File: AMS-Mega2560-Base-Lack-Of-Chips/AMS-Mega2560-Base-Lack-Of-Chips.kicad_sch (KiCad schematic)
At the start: 22 parts, among them J1 RTD1, J2 RTD2, J3 Conn_01x08, J4 Sense1, J5 Sense2, J6 AdafruitUltimateGPS, J7 Conn_02x03_Odd_Even, P1 Power, P10 CONN_01X01, P11 CONN_01X01, P12 CONN_01X01, P13 CONN_01X01, P2 Analog, P3 Analog, P4 Digital, P5 PWM, P6 PWM, P7 Communication, P8 CONN_01X01, P9 CONN_01X01

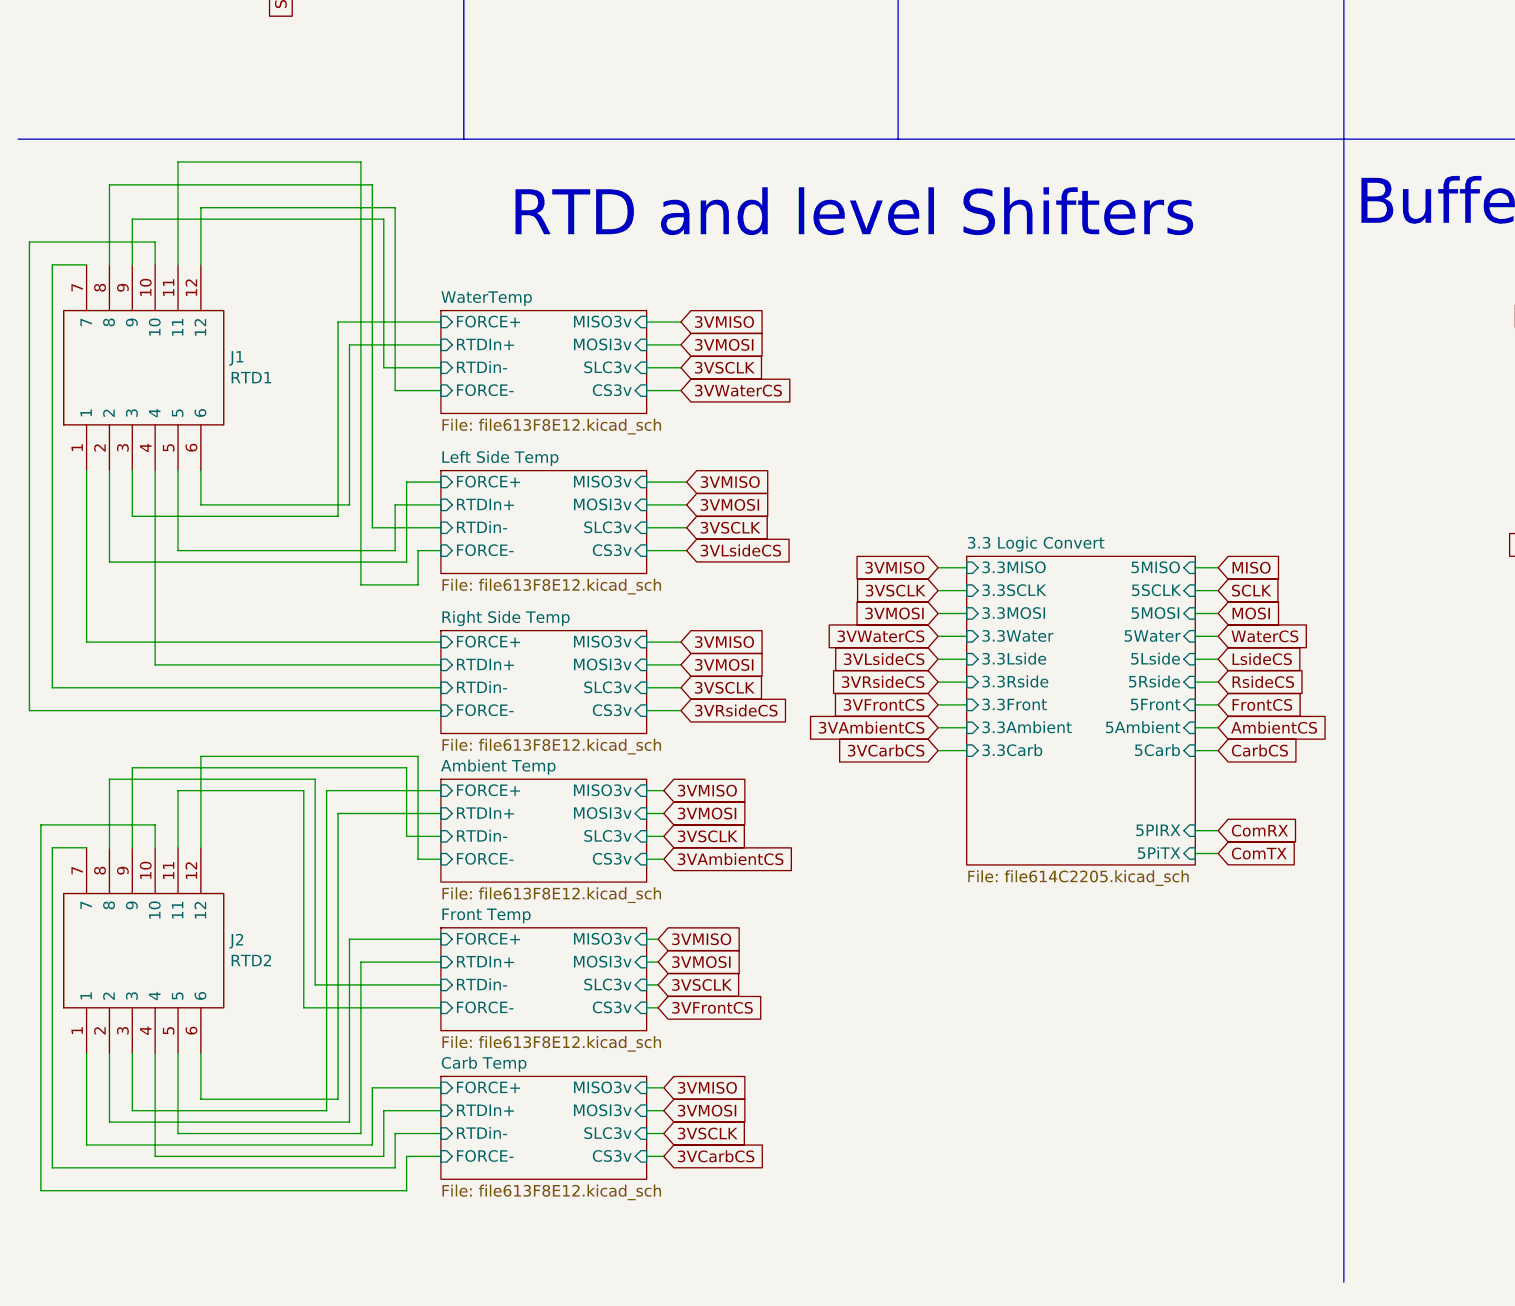
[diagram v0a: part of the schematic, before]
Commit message: replaced the RTD with adafruit Dev boards which are easy to get at the moment.
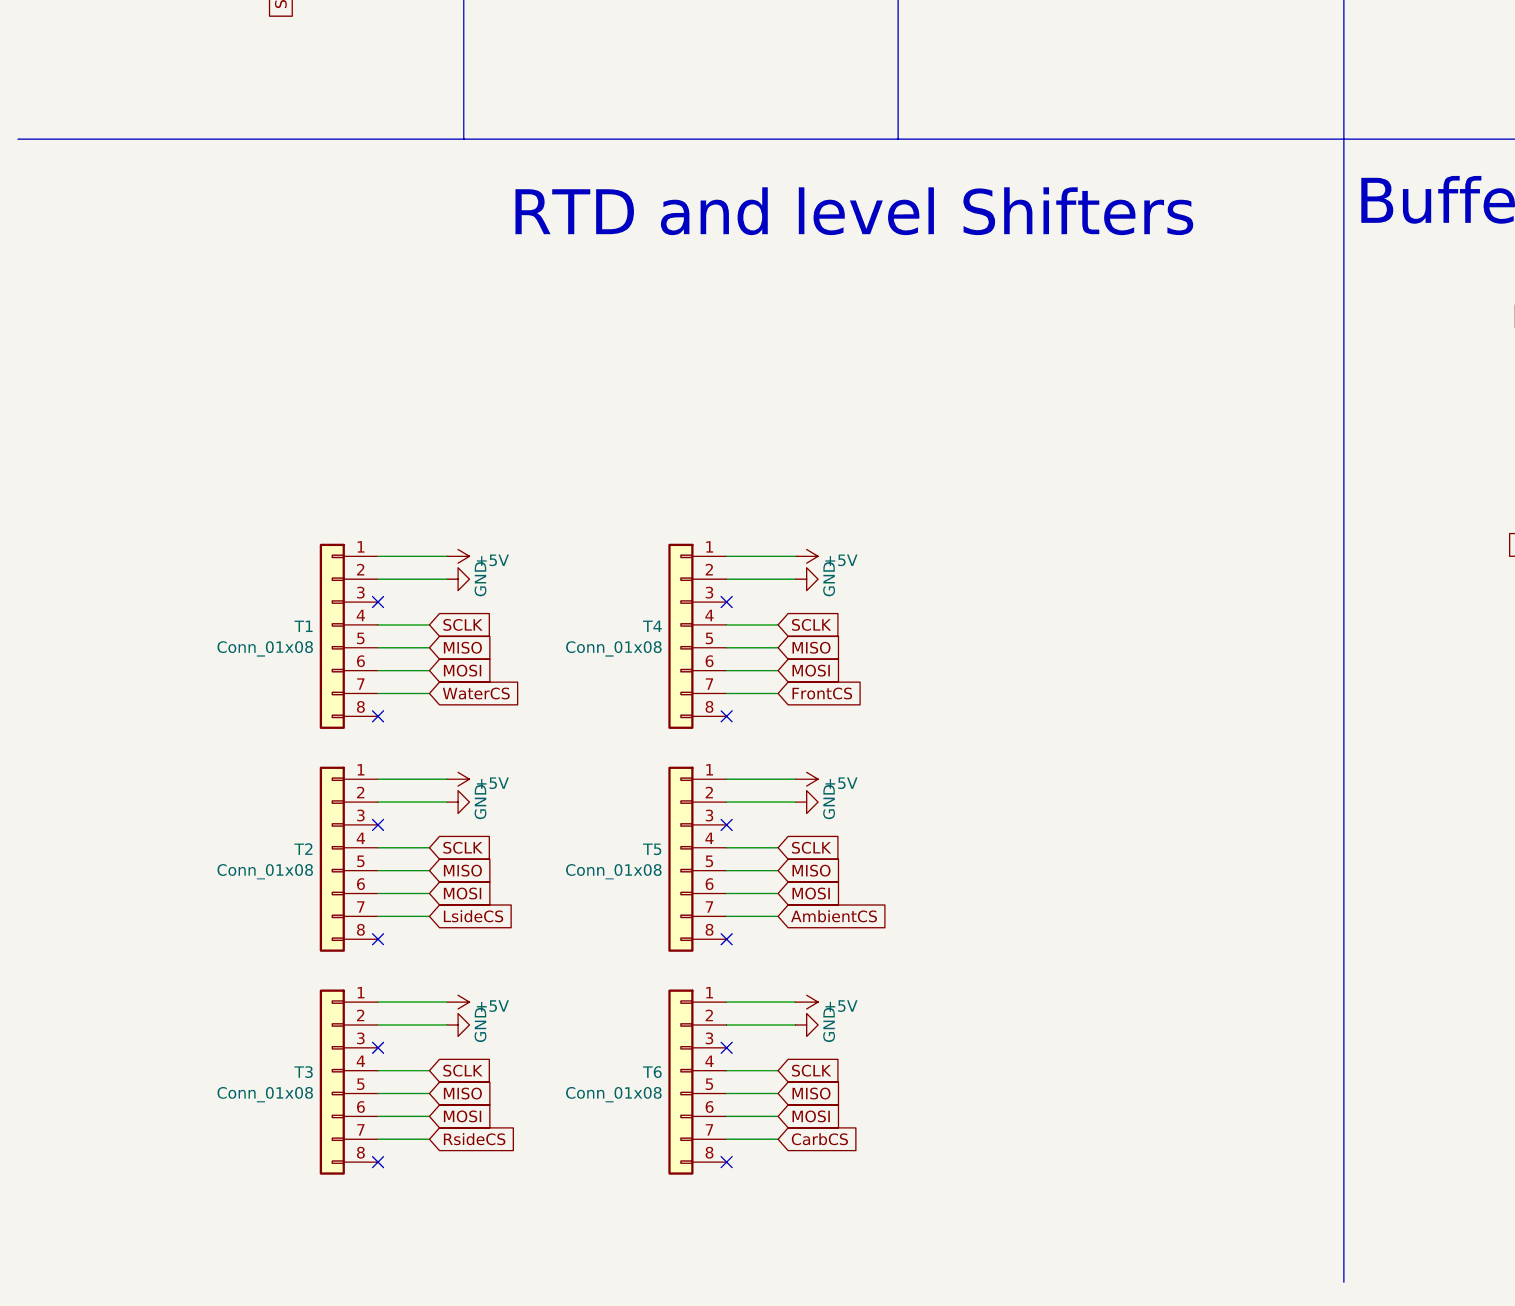
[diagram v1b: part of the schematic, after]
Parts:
- removed J1: RTD1, SamacSys_Parts:1727751, symbol SamacSys_Parts:1727751
- removed J2: RTD2, SamacSys_Parts:1727751, symbol SamacSys_Parts:1727751
- added T1, T2, T3, T4, T5, T6: Conn_01x08, Connector_PinSocket_2.54mm:PinSocket_1x08_P2.54mm_Vertical, symbol Connector_Generic:Conn_01x08
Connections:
- net +5V: now also T1.1 (Pin_1), T2.1 (Pin_1), T3.1 (Pin_1), T4.1 (Pin_1), T5.1 (Pin_1), T6.1 (Pin_1)
- net AmbientCS: now also T5.7 (Pin_7)
- net CarbCS: now also T6.7 (Pin_7)
- net FrontCS: now also T4.7 (Pin_7)
- net GND: now also T1.2 (Pin_2), T2.2 (Pin_2), T3.2 (Pin_2), T4.2 (Pin_2), T5.2 (Pin_2), T6.2 (Pin_2)
- net LsideCS: now also T2.7 (Pin_7)
- net MISO: now also T1.5 (Pin_5), T2.5 (Pin_5), T3.5 (Pin_5), T4.5 (Pin_5), T5.5 (Pin_5), T6.5 (Pin_5)
- net MOSI: now also T1.6 (Pin_6), T2.6 (Pin_6), T3.6 (Pin_6), T4.6 (Pin_6), T5.6 (Pin_6), T6.6 (Pin_6)
- net RsideCS: now also T3.7 (Pin_7)
- net SCLK: now also T1.4 (Pin_4), T2.4 (Pin_4), T3.4 (Pin_4), T4.4 (Pin_4), T5.4 (Pin_4), T6.4 (Pin_4)
- net WaterCS: now also T1.7 (Pin_7)
- no-connect marks 47 -> 59
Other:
- removed sheet 3.3 Logic Convert
- removed sheet Ambient Temp
- removed sheet Carb Temp
- removed sheet Front Temp
- removed sheet Left Side Temp
- removed sheet Right Side Temp
- removed sheet WaterTemp
